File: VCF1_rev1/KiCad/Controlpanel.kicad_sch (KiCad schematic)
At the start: 16 parts

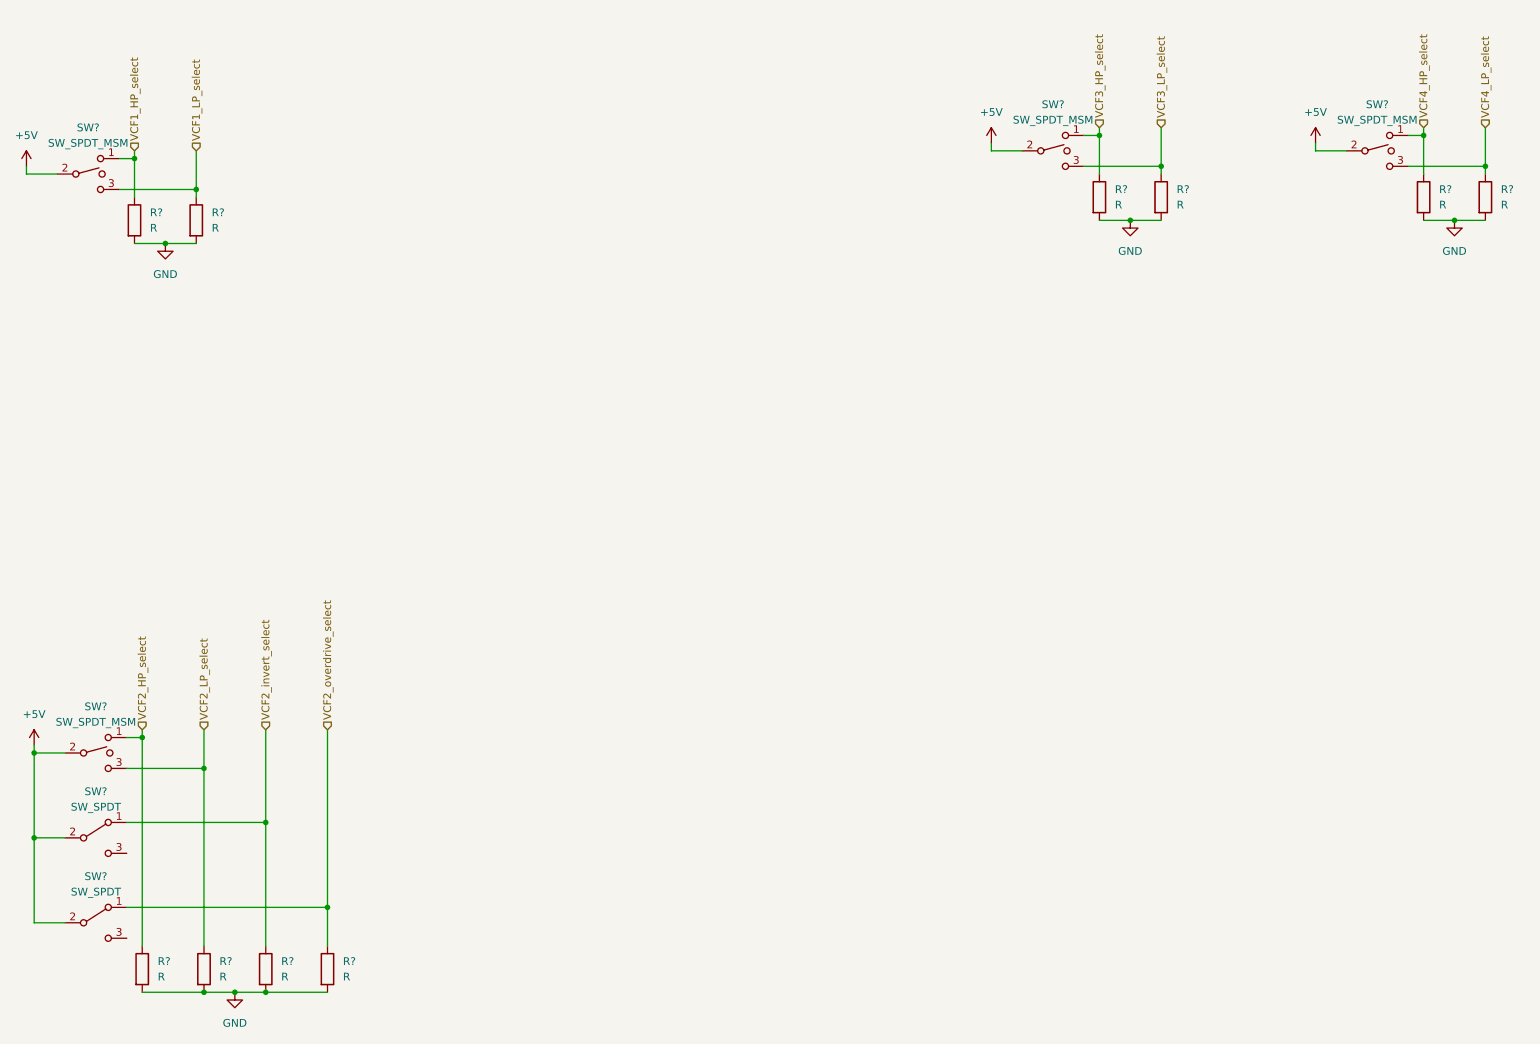
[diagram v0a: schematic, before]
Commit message: Cleaned up the first page with the overview and tried to make it a bit more readable.
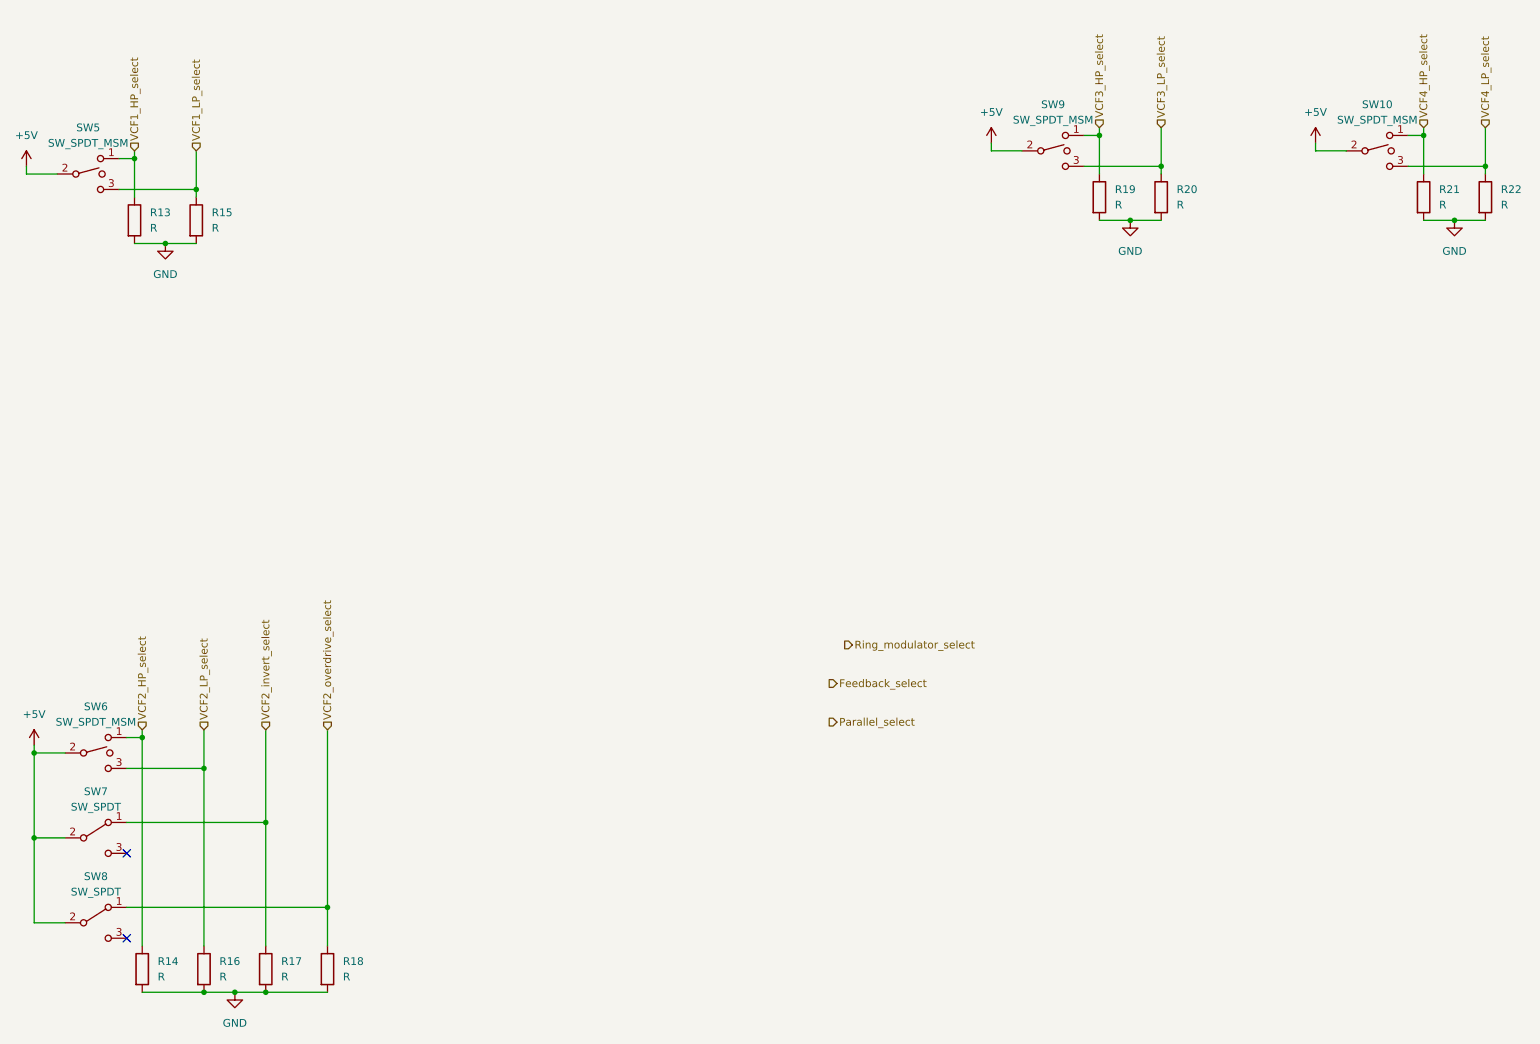
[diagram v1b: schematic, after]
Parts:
- gave numbers to parts that had none: 16
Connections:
- no-connect marks 0 -> 2

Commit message: Drew a better symbol for LM13700 because the other one was ugly.
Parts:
- R13, R14, R15, R16, R17, R18, R19, R20, R21, R22: footprint (none) -> Resistor_SMD:R_0603_1608Metric
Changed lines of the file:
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@@
 (kicad_sch (version 20210621) (generator eeschema)
   (paper "A4")
+  (junction (at 34.29 137.16) (diameter 0) (color 0 0 0 0))
+  (junction (at 62.23 139.7) (diameter 0) (color 0 0 0 0))
+  (junction (at 219.71 40.64) (diameter 0) (color 0 0 0 0))
+  (junction (at 273.05 40.64) (diameter 0) (color 0 0 0 0))
+  (junction (at 62.23 176.53) (diameter 0) (color 0 0 0 0))
+  (junction (at 209.55 35.56) (diameter 0) (color 0 0 0 0))
+  (junction (at 82.55 162.56) (diameter 0) (color 0 0 0 0))
+  (junction (at 72.39 176.53) (diameter 0) (color 0 0 0 0))
+  (junction (at 52.07 134.62) (diameter 0) (color 0 0 0 0))
+  (junction (at 72.39 148.59) (diameter 0) (color 0 0 0 0))
+  (junction (at 60.96 44.45) (diameter 0) (color 0 0 0 0))
   (junction (at 67.31 176.53) (diameter 0) (color 0 0 0 0))
-  (junction (at 72.39 148.59) (diameter 0) (color 0 0 0 0))
-  (junction (at 72.39 176.53) (diameter 0) (color 0 0 0 0))
-  (junction (at 60.96 44.45) (diameter 0) (color 0 0 0 0))
-  (junction (at 82.55 162.56) (diameter 0) (color 0 0 0 0))
-  (junction (at 62.23 176.53) (diameter 0) (color 0 0 0 0))
+  (junction (at 55.88 53.34) (diameter 0) (color 0 0 0 0))
+  (junction (at 50.8 39.37) (diameter 0) (color 0 0 0 0))
+  (junction (at 262.89 35.56) (diameter 0) (color 0 0 0 0))
   (junction (at 214.63 49.53) (diameter 0) (color 0 0 0 0))
-  (junction (at 273.05 40.64) (diameter 0) (color 0 0 0 0))
-  (junction (at 55.88 53.34) (diameter 0) (color 0 0 0 0))
   (junction (at 267.97 49.53) (diameter 0) (color 0 0 0 0))
-  (junction (at 262.89 35.56) (diameter 0) (color 0 0 0 0))
-  (junction (at 52.07 134.62) (diameter 0) (color 0 0 0 0))
   (junction (at 34.29 151.13) (diameter 0) (color 0 0 0 0))
-  (junction (at 50.8 39.37) (diameter 0) (color 0 0 0 0))
-  (junction (at 219.71 40.64) (diameter 0) (color 0 0 0 0))
-  (junction (at 209.55 35.56) (diameter 0) (color 0 0 0 0))
-  (junction (at 62.23 139.7) (diameter 0) (color 0 0 0 0))
-  (junction (at 34.29 137.16) (diameter 0) (color 0 0 0 0))
+  (no_connect (at 49.53 167.64))
   (no_connect (at 49.53 153.67))
-  (no_connect (at 49.53 167.64))
   (wire (pts (xy 49.53 148.59) (xy 72.39 148.59))
     (stroke (width 0) (type default) (color 0 0 0 0))
@@
     (stroke (width 0) (type default) (color 0 0 0 0))
   )
+  (wire (pts (xy 62.23 176.53) (xy 67.31 176.53))
+    (stroke (width 0) (type default) (color 0 0 0 0))
+  )
   (wire (pts (xy 72.39 176.53) (xy 82.55 176.53))
-    (stroke (width 0) (type default) (color 0 0 0 0))
-  )
-  (wire (pts (xy 62.23 176.53) (xy 67.31 176.53))
     (stroke (width 0) (type default) (color 0 0 0 0))
   )
@@
       (effects (font (size 1.27 1.27)) (justify left))
     )
-    (property "Footprint" "" (id 2) (at 50.292 172.72 90)
+    (property "Footprint" "Resistor_SMD:R_0603_1608Metric" (id 2) (at 50.292 172.72 90)
       (effects (font (size 1.27 1.27)) hide)
     )
@@
       (effects (font (size 1.27 1.27)) (justify left))
     )
-    (property "Footprint" "" (id 2) (at 217.932 45.72 90)
+    (property "Footprint" "Resistor_SMD:R_0603_1608Metric" (id 2) (at 217.932 45.72 90)
       (effects (font (size 1.27 1.27)) hide)
     )
@@
       (effects (font (size 1.27 1.27)) (justify left))
     )
-    (property "Footprint" "" (id 2) (at 207.772 45.72 90)
+    (property "Footprint" "Resistor_SMD:R_0603_1608Metric" (id 2) (at 207.772 45.72 90)
       (effects (font (size 1.27 1.27)) hide)
     )
@@
       (effects (font (size 1.27 1.27)) (justify left))
     )
-    (property "Footprint" "" (id 2) (at 60.452 172.72 90)
+    (property "Footprint" "Resistor_SMD:R_0603_1608Metric" (id 2) (at 60.452 172.72 90)
       (effects (font (size 1.27 1.27)) hide)
     )
@@
       (effects (font (size 1.27 1.27)) (justify left))
     )
-    (property "Footprint" "" (id 2) (at 70.612 172.72 90)
+    (property "Footprint" "Resistor_SMD:R_0603_1608Metric" (id 2) (at 70.612 172.72 90)
       (effects (font (size 1.27 1.27)) hide)
     )
@@
       (effects (font (size 1.27 1.27)) (justify left))
     )
-    (property "Footprint" "" (id 2) (at 80.772 172.72 90)
+    (property "Footprint" "Resistor_SMD:R_0603_1608Metric" (id 2) (at 80.772 172.72 90)
       (effects (font (size 1.27 1.27)) hide)
     )
@@
       (effects (font (size 1.27 1.27)) (justify left))
     )
-    (property "Footprint" "" (id 2) (at 261.112 45.72 90)
+    (property "Footprint" "Resistor_SMD:R_0603_1608Metric" (id 2) (at 261.112 45.72 90)
       (effects (font (size 1.27 1.27)) hide)
     )
@@
       (effects (font (size 1.27 1.27)) (justify left))
     )
-    (property "Footprint" "" (id 2) (at 49.022 49.53 90)
+    (property "Footprint" "Resistor_SMD:R_0603_1608Metric" (id 2) (at 49.022 49.53 90)
       (effects (font (size 1.27 1.27)) hide)
     )
@@
       (effects (font (size 1.27 1.27)) (justify left))
     )
-    (property "Footprint" "" (id 2) (at 59.182 49.53 90)
+    (property "Footprint" "Resistor_SMD:R_0603_1608Metric" (id 2) (at 59.182 49.53 90)
       (effects (font (size 1.27 1.27)) hide)
     )
@@
       (effects (font (size 1.27 1.27)) (justify left))
     )
-    (property "Footprint" "" (id 2) (at 271.272 45.72 90)
-      (effects (font (size 1.27 1.27)) hide)
-    )
+    (property "Footprint" "Resistor_SMD:R_0603_1608Metric" (id 2) (at 271.272 45.72 90)
+      (effects (font (size 1.27 1.27)) hide)
+    )

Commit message: Cleanups, better names for the sheets etc.
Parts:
- added R119, R120, R121: R, Resistor_SMD:R_0603_1608Metric, symbol Device:R
- added SW11, SW12, SW13: SW_SPDT, symbol Switch:SW_SPDT
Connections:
- net +5V: now also SW11.2 (B), SW12.2 (B), SW13.2 (B)
- net Feedback_select: now also R120.1, SW12.1 (A)
- net GND: now also R119.2, R120.2, R121.2
- net Parallel_select: now also R121.1, SW13.1 (A)
- net Ring_modulator_select: now also R119.1, SW11.1 (A)
- no-connect marks 2 -> 5
